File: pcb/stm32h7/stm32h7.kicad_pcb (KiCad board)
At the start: 4 copper layers, 59.7 x 58.9 mm, 85 parts, among them J1 USB_C_Receptacle_USB2.0_14P, J2 Battery, J3 GPS_ANT, J4 Conn_Coaxial, J5 Conn_01x40_Socket, Q1_Xtal1 32.0MHz, SW1 BOOT, SW2 SW_Push, SW3 SW_Push, U1 STM32H743VGTx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

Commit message: routing done
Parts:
- removed the C25 at (144.9, 62.8)
- added C14: 4.7uF, Capacitor_SMD:C_0402_1005Metric, F.Cu at (125.9, 99.8)
- added C22: 1uF, Capacitor_SMD:C_0402_1005Metric, F.Cu at (120.8, 97.1)
- added J6: Test Pads, custom_comps:2 Wire Pads, F.Cu at (116.4, 95.2)
- added R2: 10R, Resistor_SMD:R_0402_1005Metric, F.Cu at (122.0, 97.1)
- SW1: value BOOT -> SW_Push
- moved R7 0.25 mm to (133.8, 51.6)
- moved R6 0.25 mm to (126.6, 51.4)
- moved SW3 0.18 mm to (127.6, 62.4)
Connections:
- SW1 pad 1: GND -> BTN
- SW1 pad 2: GP0 -> GND
- SW2 pad 1: GND -> NRST
- SW2 pad 3: (no net) -> GND
- SW2 pad 4: (no net) -> GND
- SW3 pad 1: Net-(U1-BOOT0) -> +3V3
- SW3 pad 3: (no net) -> Net-(U1-BOOT0)
- SW3 pad 4: (no net) -> Net-(U1-BOOT0)
- U1 pad 24: GND -> Net-(J6-Pin_2)
- U1 pad 32: GND -> Net-(J6-Pin_1)
- U1 pad 33: GND -> BTN
- Y1 pad 1: GND -> PH0
- Y1 pad 2: PH0 -> GND
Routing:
- net SCL: track 3.43 -> 100.4 mm, vias 0 -> 7
- net SDA: track 5.06 -> 66.6 mm, vias 0 -> 4
- net LoRa_NSS: track 0.00 -> 47.2 mm, vias 0 -> 4
- net VBUS: track 32.1 -> 68.0 mm, vias 0 -> 6
- net GND: track 67.3 -> 101.7 mm, vias 251 -> 453
- net BTN: track 0.00 -> 30.7 mm, vias 0 -> 2
- net MOSI: track 42.8 -> 72.1 mm, vias 3 -> 9
- net QSPI_D2: track 6.78 -> 31.9 mm
- net LCD_RST: track 27.9 -> 47.6 mm, vias 2 -> 8
- net INT_MAG: track 3.10 -> 20.9 mm, vias 2 -> 4
- net LCD_G1: track 30.5 -> 47.1 mm, vias 2 -> 8
- net LCD_R2: track 38.9 -> 55.2 mm, vias 2 -> 8
- net LCD_CS: track 4.04 -> 20.0 mm, vias 0 -> 2
- net Net-(J6-Pin_2): track 0.00 -> 15.9 mm, vias 0 -> 2
- net LCD_B2: track 28.2 -> 42.8 mm
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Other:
- board text added: "Festival Tracker v0.3 Big Z and Lil T Productions"
- board text added: "PA2"
- board text added: "PC4"
- board text removed: "Festival Tracker v0.2 Big Z and Lil T Productions"

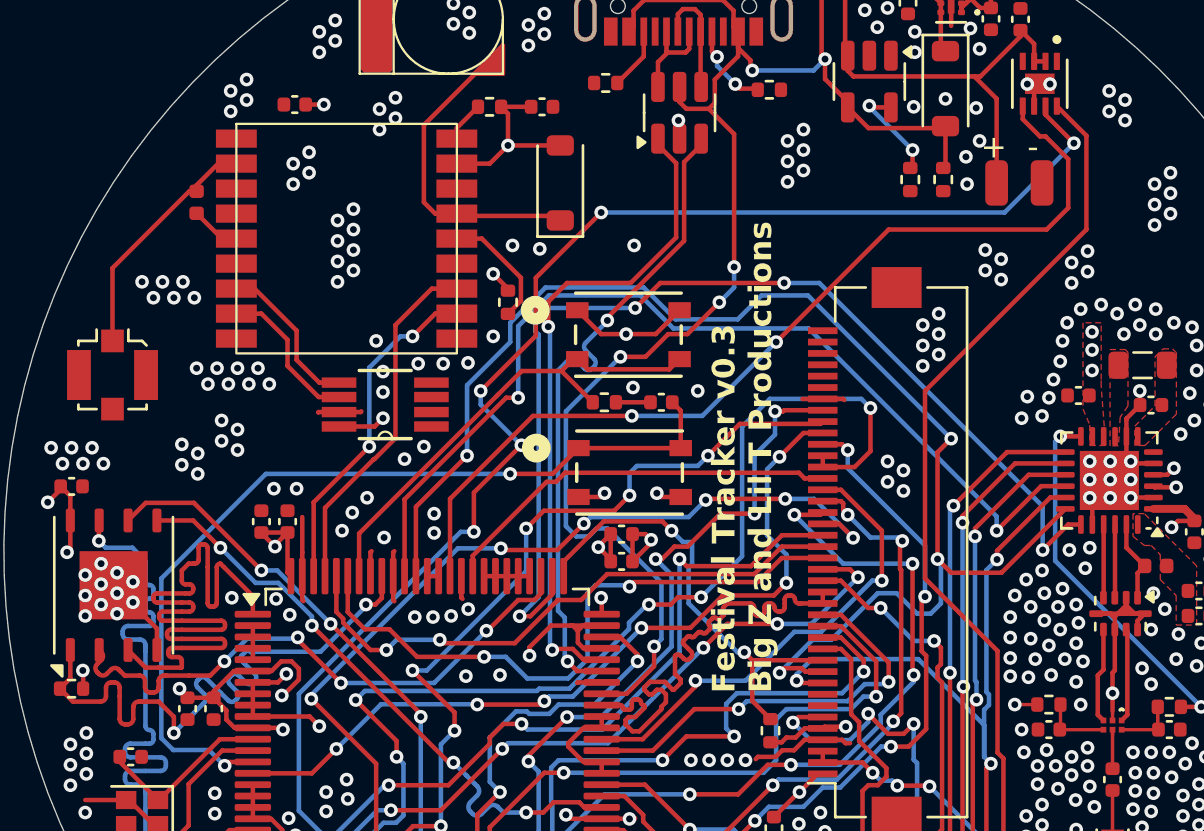
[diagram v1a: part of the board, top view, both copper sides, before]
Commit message: fixed some footprints and added power switching mosfet for gps
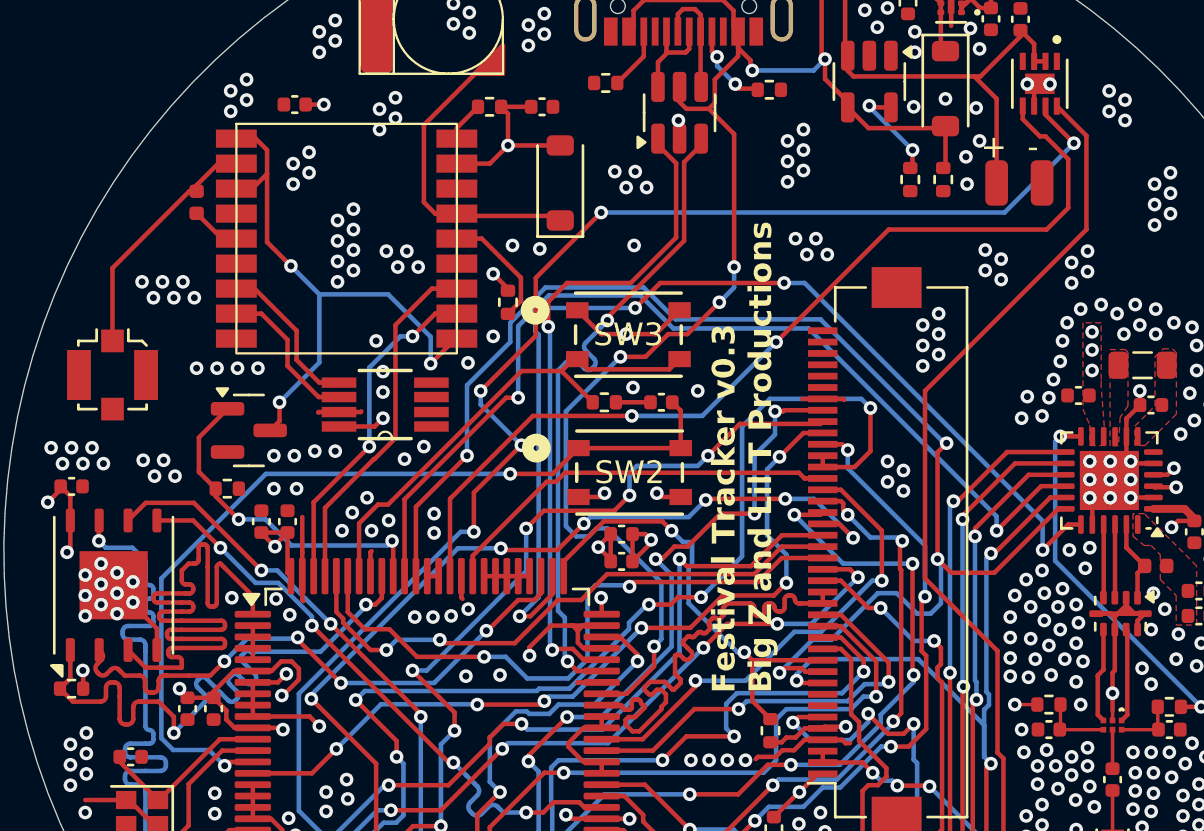
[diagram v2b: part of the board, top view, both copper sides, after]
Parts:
- added Q1: DMG3414U, Package_TO_SOT_SMD:SOT-23, F.Cu at (110.9, 66.6)
- added R10: 10k, Resistor_SMD:R_0402_1005Metric, F.Cu at (110.0, 69.2)
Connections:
- ATGM336H1 pad 1: GND -> Net-(ATGM336H1-GND)
- U1 pad 91: GND -> GPS_ON
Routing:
- net Net-(ATGM336H1-GND): track 0.00 -> 25.8 mm, vias 0 -> 3
- net GPS_ON: track 0.00 -> 15.0 mm, vias 0 -> 2
- net GND: track 101.7 -> 99.5 mm, vias 453 -> 460
- net SCK: track 62.3 -> 61.0 mm

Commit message: is it finally done or am i going insane
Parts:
- removed R14: 10K, Resistor_SMD:R_0402_1005Metric
- added C38: 100nF, Capacitor_SMD:C_0402_1005Metric, F.Cu at (143.1, 91.3)
- added C39: 10uF, Capacitor_SMD:C_0402_1005Metric, F.Cu at (141.9, 91.3)
- added D4: MBR0540, Diode_SMD:D_SOD-123, F.Cu at (133.2, 54.6)
- added Q2: IRLML2244, Package_TO_SOT_SMD:SOT-23, F.Cu at (136.6, 55.9)
- added R11: 10k, Resistor_SMD:R_0402_1005Metric, F.Cu at (135.6, 53.4)
- moved R16 2.60 mm to (135.6, 89.6)
- moved R15 2.55 mm to (135.6, 92.2)
- moved R7 0.45 mm to (133.8, 51.2)
- moved R6 0.15 mm to (126.6, 51.2)
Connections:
- C12 pad 2: +3V3 -> LDO_OUT
- R16 pad 2: SDA -> SCL
- R17 pad 2: SCL -> SDA
- U1 pad 16: GND -> PWR_ON
- U2 pad 1: +3V3 -> LDO_OUT
- U2 pad 2: +3V3 -> LDO_OUT
- U2 pad 4: +3V3 -> LDO_OUT
- U8 pad 1: SDA -> SCL
- U8 pad 2: /Accel & Magnetometer/CS_XL -> /Accel & Magnetometer/CS_MAG
- U8 pad 4: SCL -> SDA
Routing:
- net BTN: track 30.7 -> 87.7 mm, vias 2 -> 5
- net PWR_ON: track 0.00 -> 52.5 mm, vias 0 -> 4
- net LDO_OUT: track 0.00 -> 17.3 mm, vias 0 -> 2
- net +3V3: track 101.3 -> 96.5 mm, vias 33 -> 32
- net /Accel & Magnetometer/CS_XL: track 4.68 -> 0.00 mm
- net FG_NALERT: track 41.4 -> 38.4 mm
- net SDA: track 66.6 -> 68.7 mm, vias 4 -> 5
- net Net-(ATGM336H1-GND): track 25.8 -> 24.5 mm
- net GND: track 99.5 -> 100.7 mm, vias 460 -> 462
- net LCD_G1: track 47.1 -> 46.1 mm
- net SCL: track 100.4 -> 99.7 mm, vias 7 -> 9
- net MOSI: track 72.2 -> 71.7 mm, vias 9 -> 7
- net VBUS: track 68.0 -> 68.3 mm, vias 6 -> 4
- net /Accel & Magnetometer/CS_MAG: track 3.79 -> 3.88 mm, vias 0 -> 2
- net LoRa_RST: track 39.2 -> 39.3 mm, vias 4 -> 6
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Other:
- board text removed: "please just show up on the computer. make the little noise and let me program you. you know you want it. it's not even that hard. communicate over usb like a good little board."

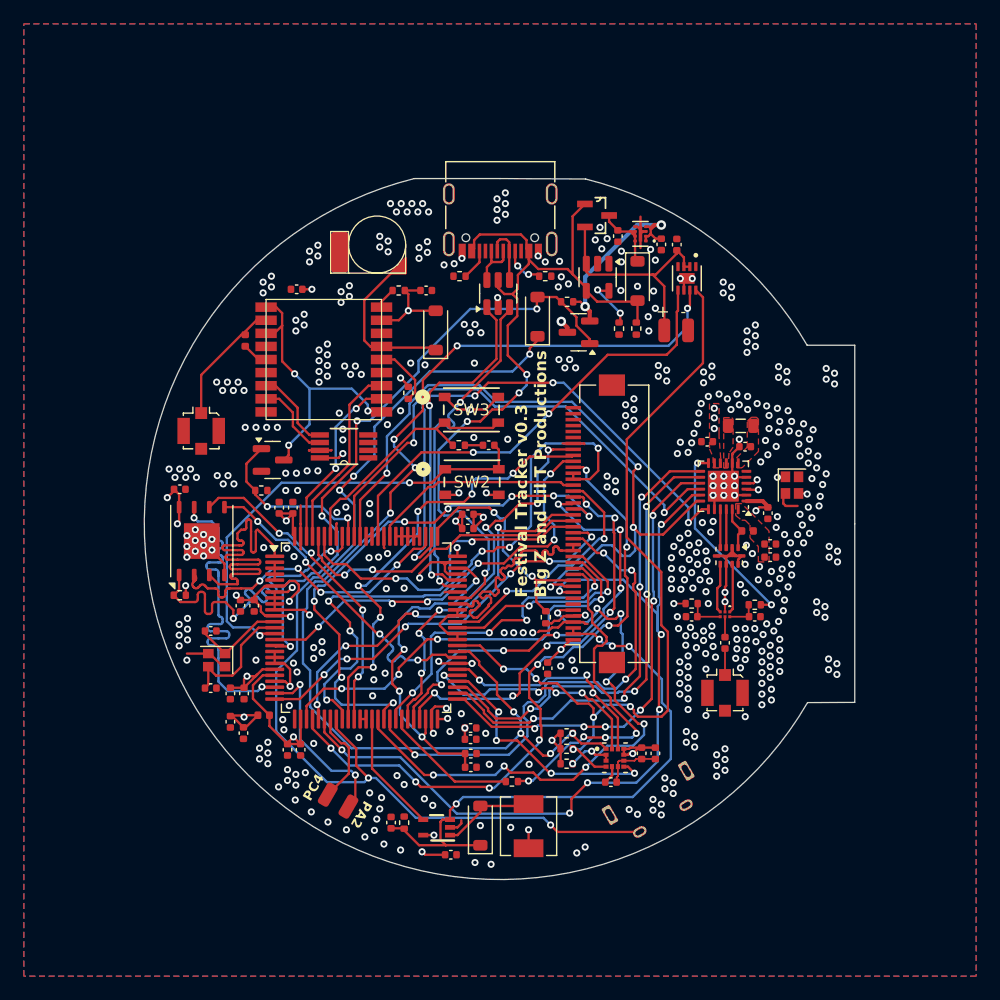
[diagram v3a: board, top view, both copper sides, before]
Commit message: using EN on the LDO for power switch now
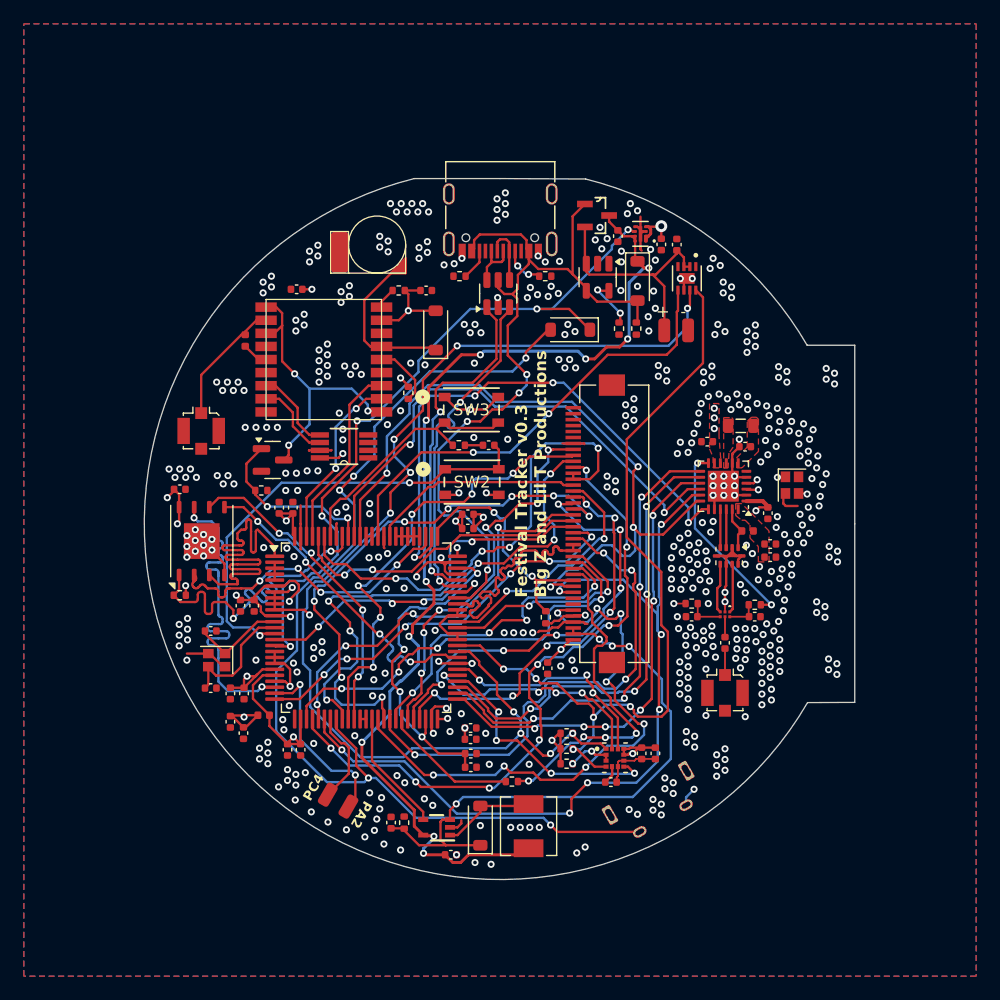
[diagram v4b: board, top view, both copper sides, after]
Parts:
- removed Q2: IRLML2244, Package_TO_SOT_SMD:SOT-23
- removed R11: 10k, Resistor_SMD:R_0402_1005Metric
- moved D4 2.96 mm to (135.9, 55.7), turned to 180 degrees
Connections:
- C12 pad 2: LDO_OUT -> +3V3
- C14 pad 1: +3V3 -> VCC
- D4 pad 1: BTN -> LDO_EN
- D4 pad 2: PWR_ON -> BTN
- L1 pad 1: +3V3 -> VCC
- SW1 pad 2: GND -> +3V3
- U1 pad 16: PWR_ON -> LDO_EN
- U11 pad 5: +3V3 -> VCC
- U2 pad 1: LDO_OUT -> +3V3
- U2 pad 2: LDO_OUT -> +3V3
- U2 pad 4: LDO_OUT -> +3V3
- U2 pad 6: VCC -> LDO_EN
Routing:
- net VCC: track 6.47 -> 88.6 mm, vias 0 -> 10
- net LDO_EN: track 0.00 -> 61.3 mm, vias 0 -> 5
- net PWR_ON: track 52.5 -> 0.00 mm, vias 4 -> 0
- net LDO_OUT: track 17.3 -> 0.00 mm, vias 2 -> 0
- net GND: track 100.7 -> 103.3 mm, vias 462 -> 484
- net BTN: track 87.7 -> 89.3 mm
- net +3V3: track 96.5 -> 97.4 mm, vias 32 -> 30
- net LCD_G1: track 46.1 -> 45.4 mm

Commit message: fixed some wiring
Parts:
- added R11: 0R, Resistor_SMD:R_0402_1005Metric, F.Cu at (148.4, 52.9)
- moved C14 2.08 mm to (123.8, 99.7)
- moved R2 0.10 mm to (122.0, 97.1), turned to -90 degrees
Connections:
- C22 pad 2: BL_OUT -> BL_ANODE
- D3 pad 1: BL_OUT -> BL_ANODE
- J5 pad 1: +3V3 -> BL_ANODE
- J5 pad 2: BL_OUT -> BL_CATHODE
- J5 pad 3: BL_OUT -> BL_CATHODE
- R2 pad 1: BL_OUT -> GND
- R2 pad 2: GND -> BL_CATHODE
- U11 pad 3: BL_OUT -> BL_CATHODE
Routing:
- net BL_OUT: track 48.9 -> 0.00 mm, vias 4 -> 0
- net BL_CATHODE: track 0.00 -> 45.3 mm, vias 0 -> 6
- net BL_ANODE: track 0.00 -> 32.3 mm, vias 0 -> 6
- net LDO_EN: track 61.3 -> 71.5 mm, vias 5 -> 6
- net VCC: track 88.6 -> 95.3 mm, vias 10 -> 9
- net +3V3: track 97.4 -> 95.2 mm
- net MOSI: track 71.7 -> 70.5 mm
- net BTN: track 89.3 -> 90.1 mm, vias 5 -> 7
- net SDA: track 68.7 -> 68.0 mm
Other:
- board text added: "BOOT0"
- board text added: "LDO_EN"
- board text added: "RESET"

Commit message: idek what i did
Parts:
- moved C14 0.65 mm to (124.5, 99.6)
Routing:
- net +3V3: track 95.2 -> 96.1 mm
- net VCC: track 95.3 -> 94.5 mm
- net BL_CATHODE: track 45.3 -> 46.1 mm
- net GND: vias 484 -> 488

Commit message: finished pcb, ordered v0.3
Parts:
- C1, C2: value 200nF -> 220nF
- C4, C5: value 3.9pF -> 8pF
- moved C38 0.50 mm to (143.1, 90.8)
- moved C39 0.50 mm to (141.9, 90.8)
- moved BT1 0.32 mm to (119.9, 48.7)
- moved C33 0.08 mm to (139.4, 93.7)
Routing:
- net LCD_R2: track 55.6 -> 50.9 mm
- net LCD_G5: track 17.9 -> 22.1 mm
- net BL_CATHODE: track 46.1 -> 49.2 mm
- net Net-(J5-Pin_12): track 28.8 -> 25.9 mm
- net GND: track 103.7 -> 106.5 mm, vias 488 -> 494
- net LCD_RST: track 47.8 -> 45.3 mm
- net LCD_HSYNC: track 18.5 -> 20.1 mm
- net LCD_B4: track 27.6 -> 26.2 mm
- net +3V3: track 96.1 -> 97.5 mm, vias 30 -> 31
- net INT_MAG: track 20.9 -> 20.1 mm
- net SCL: track 99.9 -> 99.0 mm
- net FG_NALERT: track 38.4 -> 39.1 mm
- net SCK: track 60.7 -> 61.4 mm
- net QSPI_CLK: track 26.8 -> 27.4 mm
- net BTN: track 89.6 -> 89.4 mm, vias 7 -> 6
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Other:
- board text added: "It is not the critic who counts; not the man who points out how the strong man stumbles, or where the doer of deeds could have done them better. The credit belongs to the man who is actually in the arena, whose face is marred by dust and sweat and blood; who strives valiantly; who errs, who comes short again and again, because there is no effort without error and shortcoming; but who does actuall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"
- board text removed: "3"
- board text removed: ":"
